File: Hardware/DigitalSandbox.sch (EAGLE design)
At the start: 80 parts, among them J1 AVR_SPI_PRG_6NS, Q1 MOSFET-N, Q2 MOSFET-P, U1 MCP73831, U2 ATMEGA328, U3 C2031N-1A2-B10K-GP, U4 MCP9700, U5 FT232RLSSOP, U6 LIGHTSENSORALS, U7 V_REG_LDOSMD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

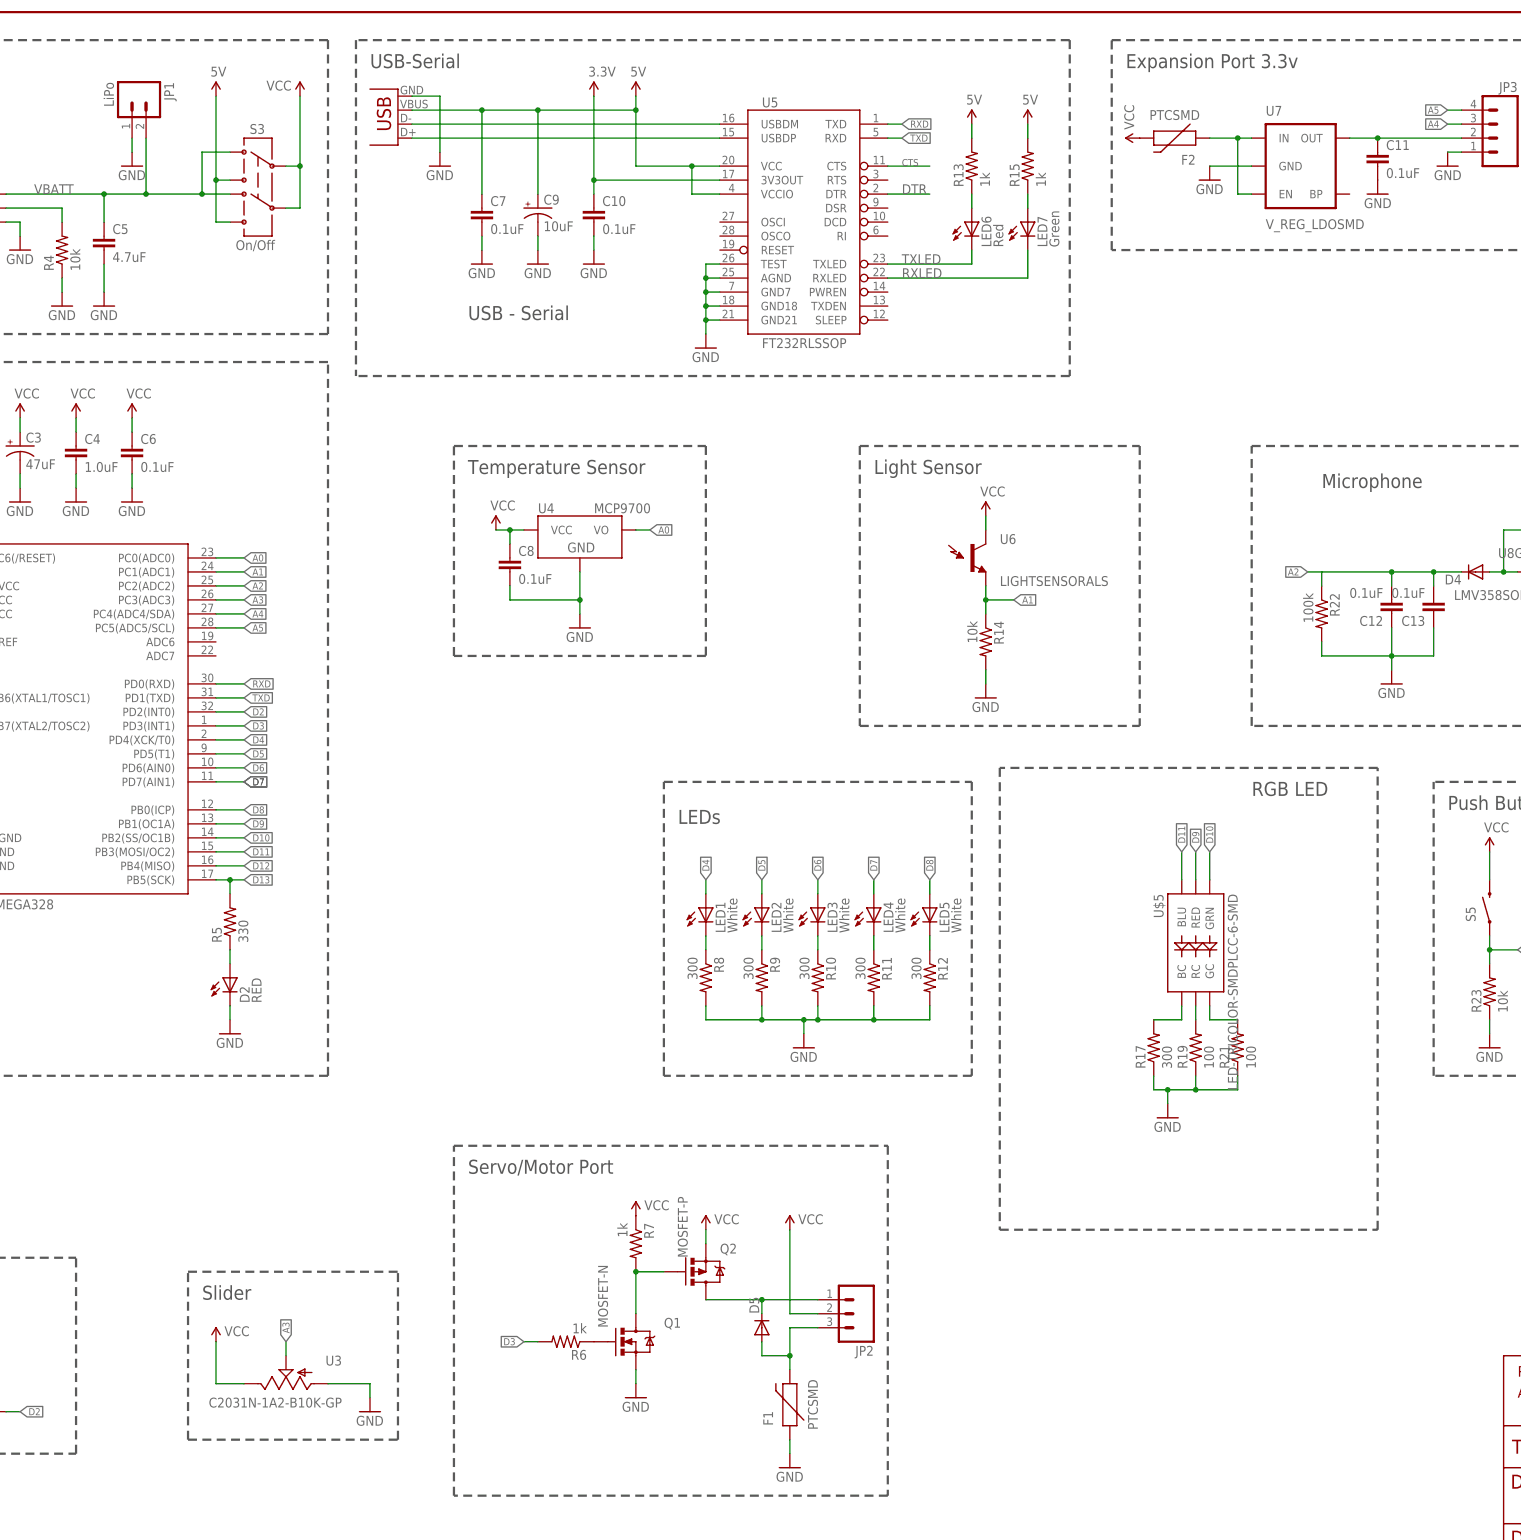
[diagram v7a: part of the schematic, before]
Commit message: updated Sparkle ID's
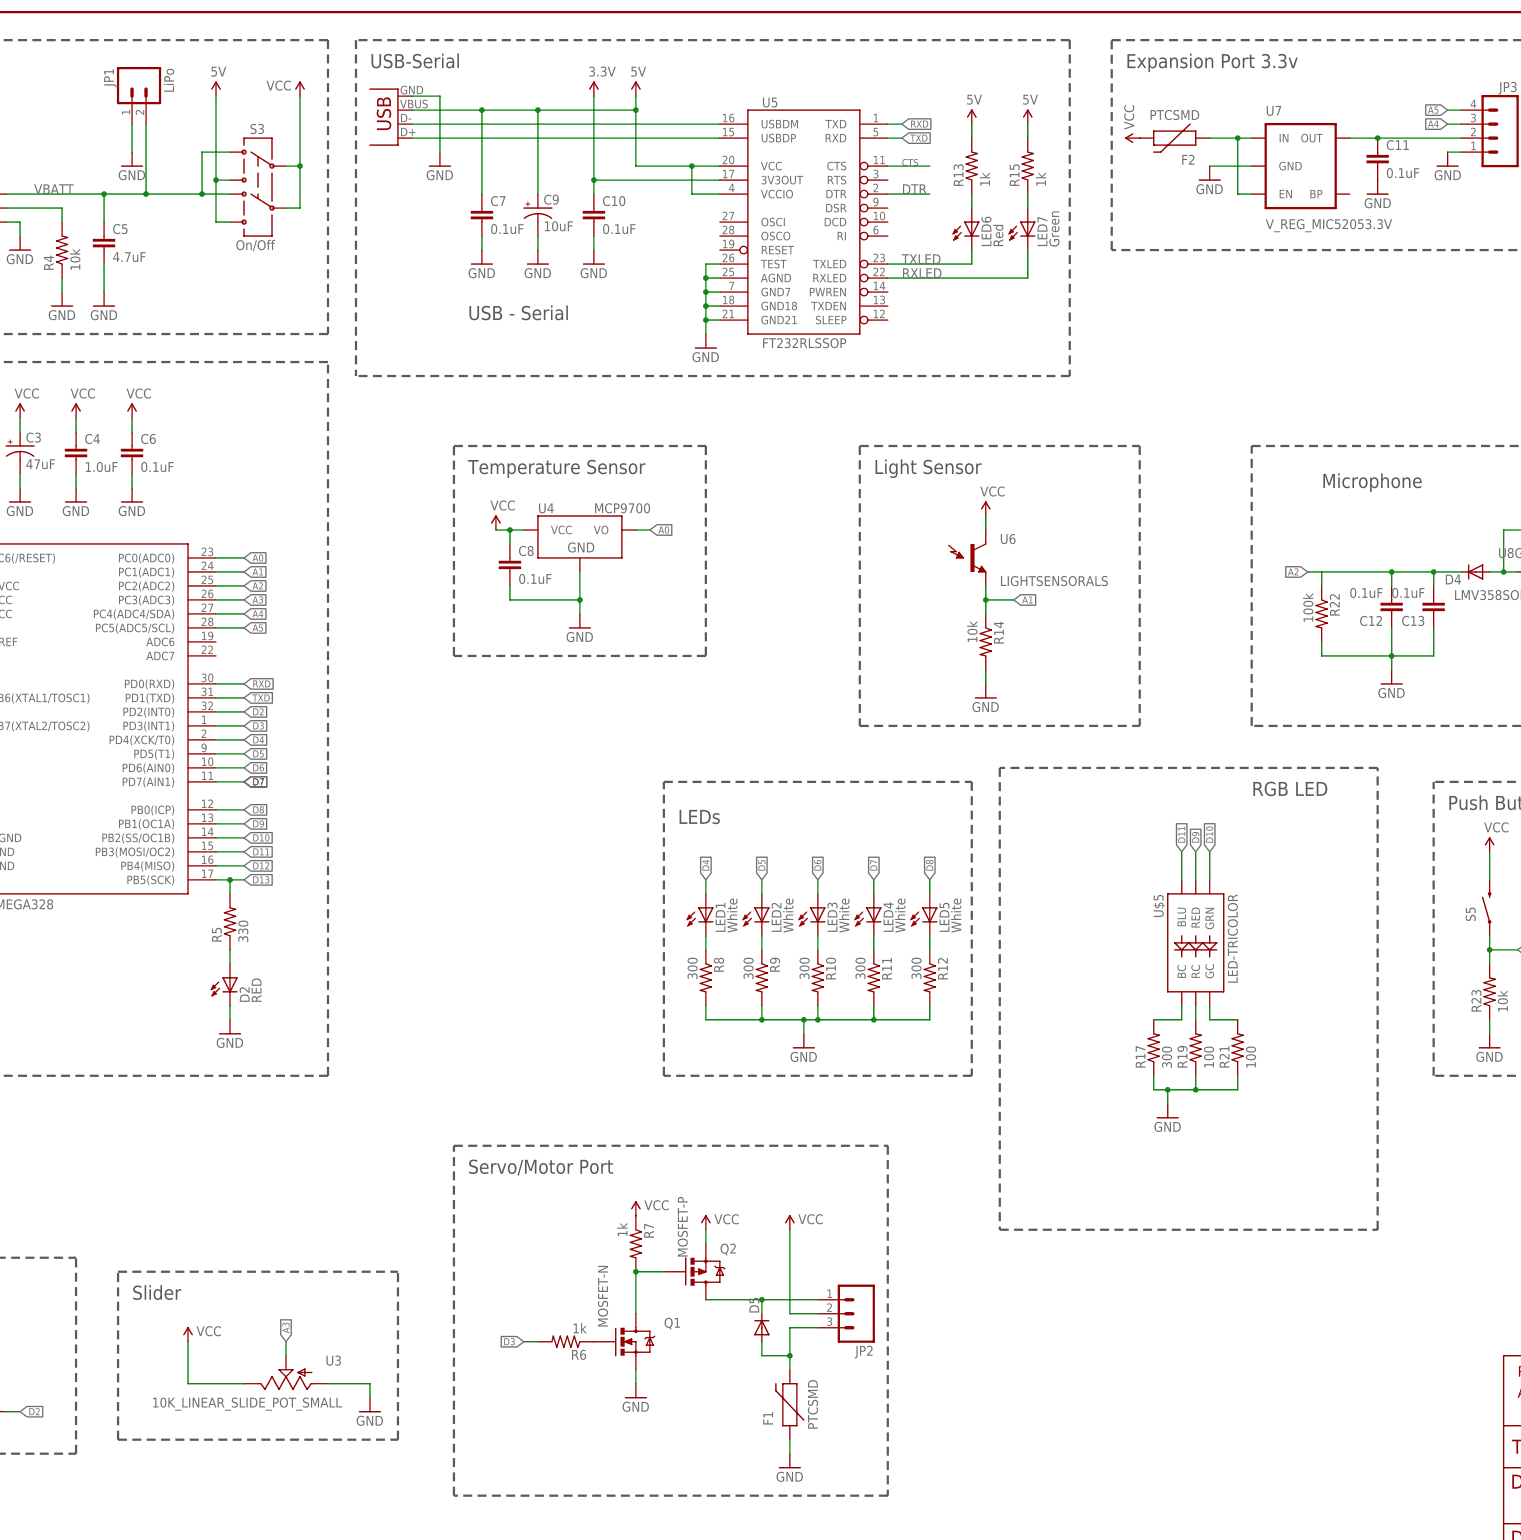
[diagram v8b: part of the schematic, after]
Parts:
- C4: device SparkFun:CAP0603-CAP -> SparkFun-Capacitors:1.0UF-16V-10%(0603)
- JP1: device SparkFun:M02-JST-2MM-SMT -> SparkFun-Connectors:M02-JST-2MM-SMT
- U$5: value LED-TRICOLOR-SMDPLCC-6-SMD -> LED-TRICOLOR; device Testing:LED-TRICOLOR-SMDPLCC-6-SMD -> SparkFun-LED:LED-TRICOLOR-NO-COMPLCC-6-SMD
- U3: value C2031N-1A2-B10K-GP -> 10K_LINEAR_SLIDE_POT_SMALL; device C2031N-1A2-B10K-GP:C2031N-1A2-B10K-GP -> SparkFun-Resistors:10K_LINEAR_SLIDE_POT_SMALL
- U4: device SparkFun:MCP9700SMD -> SparkFun-Sensors:MCP9700SMD
- U7: value V_REG_LDOSMD -> V_REG_MIC52053.3V; device SparkFun-PowerIC:V_REG_LDOSMD -> SparkFun-PowerIC:V_REG_MIC52053.3V
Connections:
- net GND: now also JP1.2; no longer JP1.1
- net VBATT: now also JP1.1; no longer JP1.2
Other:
- moved on the sheet: JP1
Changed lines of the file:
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@@
 <layer number="54" name="bGND_GNDA" color="1" fill="9" visible="no" active="no"/>
 <layer number="56" name="wert" color="7" fill="1" visible="no" active="no"/>
+<layer number="57" name="tCAD" color="7" fill="1" visible="no" active="no"/>
 <layer number="91" name="Nets" color="2" fill="1" visible="yes" active="yes"/>
 <layer number="92" name="Busses" color="1" fill="1" visible="yes" active="yes"/>
@@
 <layer number="97" name="Info" color="7" fill="1" visible="yes" active="yes"/>
 <layer number="98" name="Guide" color="6" fill="1" visible="yes" active="yes"/>
+<layer number="99" name="SpiceOrder" color="7" fill="1" visible="yes" active="yes"/>
 <layer number="100" name="Muster" color="7" fill="1" visible="no" active="no"/>
 <layer number="101" name="Patch_Top" color="12" fill="4" visible="yes" active="yes"/>
@@
 <layer number="132" name="bAdjust" color="7" fill="1" visible="yes" active="yes"/>
 <layer number="144" name="Drill_legend" color="7" fill="1" visible="yes" active="yes"/>
+<layer number="150" name="Notes" color="7" fill="1" visible="yes" active="yes"/>
 <layer number="151" name="HeatSink" color="7" fill="1" visible="yes" active="yes"/>
 <layer number="152" name="_bDocu" color="7" fill="1" visible="yes" active="yes"/>
+<layer number="153" name="FabDoc1" color="7" fill="1" visible="yes" active="yes"/>
+<layer number="154" name="FabDoc2" color="7" fill="1" visible="yes" active="yes"/>
+<layer number="155" name="FabDoc3" color="7" fill="1" visible="yes" active="yes"/>
 <layer number="199" name="Contour" color="7" fill="1" visible="yes" active="yes"/>
 <layer number="200" name="200bmp" color="1" fill="10" visible="no" active="no"/>
@@
 <part name="Y1" library="SparkFun-FreqCtrl" deviceset="RESONATOR" device="8MHZ" value="8MHz"/>
 <part name="GND9" library="SparkFun" deviceset="GND" device=""/>
-<part name="JP1" library="SparkFun" deviceset="M02" device="-JST-2MM-SMT" value="LiPo"/>
+<part name="JP1" library="SparkFun-Connectors" deviceset="M02" device="-JST-2MM-SMT" value="LiPo"/>
 <part name="S3" library="SparkFun-Electromechanical" deviceset="SWITCH-DPDT" device="AYZ0202" value="On/Off"/>
 <part name="GND18" library="supply1" deviceset="GND" device=""/>
@@
 <part name="S1" library="SparkFun-Electromechanical" deviceset="TAC_SWITCH" device="SMD" value="Reset"/>
 <part name="GND13" library="supply1" deviceset="GND" device=""/>
-<part name="U4" library="SparkFun" deviceset="MCP9700" device="SMD" value="MCP9700"/>
+<part name="U4" library="SparkFun-Sensors" deviceset="MCP9700" device="SMD" value="MCP9700"/>
 <part name="C8" library="SparkFun-Capacitors" deviceset="0.1UF-25V(+80/-20%)(0603)" device="" value="0.1uF"/>
 <part name="S2" library="SparkFun-Electromechanical" deviceset="SWITCH-DPDT" device="AYZ0202"/>
@@
 <part name="R11" library="SparkFun-Resistors" deviceset="300OHM-1/10W-1%(0603)" device="" value="300"/>
 <part name="R12" library="SparkFun-Resistors" deviceset="300OHM-1/10W-1%(0603)" device="" value="300"/>
-<part name="U3" library="C2031N-1A2-B10K-GP" deviceset="C2031N-1A2-B10K-GP" device=""/>
+<part name="U3" library="SparkFun-Resistors" deviceset="10K_LINEAR_SLIDE_POT_SMALL" device=""/>
 <part name="R17" library="SparkFun-Resistors" deviceset="300OHM-1/10W-1%(0603)" device="" value="300"/>
 <part name="R19" library="SparkFun-Resistors" deviceset="100OHM1/10W1%(0603)" device="" value="100"/>
@@
 <part name="C6" library="SparkFun-Capacitors" deviceset="0.1UF-25V(+80/-20%)(0603)" device="" value="0.1uF"/>
 <part name="C1" library="SparkFun-Capacitors" deviceset="0.1UF-25V(+80/-20%)(0603)" device="" value="0.1uF"/>
-<part name="C4" library="SparkFun" deviceset="CAP" device="0603-CAP" value="1.0uF"/>
+<part name="C4" library="SparkFun-Capacitors" deviceset="1.0UF-16V-10%(0603)" device="" value="1.0uF"/>
 <part name="GND8" library="SparkFun" deviceset="GND" device=""/>
 <part name="R3" library="SparkFun-Resistors" deviceset="10KOHM1/10W1%(0603)" device="0603" value="10k"/>
@@
 <part name="JP3" library="SparkFun-Connectors" deviceset="M04" device="SMD_STRAIGHT_COMBO"/>
 <part name="GND31" library="SparkFun" deviceset="GND" device=""/>
-<part name="U7" library="SparkFun-PowerIC" deviceset="V_REG_LDO" device="SMD"/>
+<part name="U7" library="SparkFun-PowerIC" deviceset="V_REG_MIC5205" device="3.3V"/>
 <part name="GND32" library="SparkFun" deviceset="GND" device=""/>
 <part name="P+19" library="SparkFun" deviceset="VCC" device=""/>
@@
 <part name="D5" library="SparkFun-DiscreteSemi" deviceset="DIODE" device="SOD"/>
 <part name="D2" library="SparkFun-LED" deviceset="LED-RED" device="1206" value="RED"/>
-<part name="U$5" library="Testing" deviceset="LED-TRICOLOR-SMD" device="PLCC-6-SMD"/>
+<part name="U$5" library="SparkFun-LED" deviceset="LED-TRICOLOR-NO-COM" device="PLCC-6-SMD" value="LED-TRICOLOR"/>
 <part name="S5" library="SparkFun-Electromechanical" deviceset="SWITCH-MOMENTARY-2" device="SMD-4"/>
 <part name="GND34" library="SparkFun" deviceset="GND" device=""/>
@@
 <text x="124.46" y="269.24" size="2.54" layer="97">USB-Serial</text>
 <text x="142.24" y="68.58" size="2.54" layer="97">Servo/Motor Port</text>
-<text x="93.98" y="48.26" size="2.54" layer="97" rot="MR180">Slider</text>
+<text x="81.28" y="48.26" size="2.54" layer="97" rot="MR180">Slider</text>
 <text x="320.04" y="134.62" size="2.54" layer="97">Push Button</text>
 <text x="22.86" y="48.26" size="2.54" layer="97" rot="MR180">Slide Switch</text>
@@
 <wire x1="71.12" y1="17.78" x2="71.12" y2="53.34" width="0.4064" layer="97" style="shortdash"/>
 <wire x1="20.32" y1="53.34" x2="71.12" y2="53.34" width="0.4064" layer="97" style="shortdash"/>
-<wire x1="91.44" y1="50.8" x2="129.54" y2="50.8" width="0.4064" layer="97" style="shortdash"/>
-<wire x1="91.44" y1="20.32" x2="91.44" y2="50.8" width="0.4064" layer="97" style="shortdash"/>
+<wire x1="78.74" y1="50.8" x2="129.54" y2="50.8" width="0.4064" layer="97" style="shortdash"/>
+<wire x1="78.74" y1="20.32" x2="78.74" y2="50.8" width="0.4064" layer="97" style="shortdash"/>
 <wire x1="129.54" y1="20.32" x2="129.54" y2="50.8" width="0.4064" layer="97" style="shortdash"/>
-<wire x1="91.44" y1="20.32" x2="129.54" y2="20.32" width="0.4064" layer="97" style="shortdash"/>
+<wire x1="78.74" y1="20.32" x2="129.54" y2="20.32" width="0.4064" layer="97" style="shortdash"/>
 <wire x1="213.36" y1="200.66" x2="213.36" y2="149.86" width="0.4064" layer="97" style="shortdash"/>
 <wire x1="213.36" y1="149.86" x2="264.16" y2="149.86" width="0.4064" layer="97" style="shortdash"/>
@@
 </instance>
 <instance part="GND9" gate="1" x="33.02" y="147.32"/>
-<instance part="JP1" gate="G$1" x="81.28" y="264.16" rot="R270"/>
+<instance part="JP1" gate="G$1" x="83.82" y="266.7" rot="MR270"/>
 <instance part="S3" gate="G$1" x="104.14" y="248.92" smashed="yes" rot="MR0">
 <attribute name="NAME" x="102.616" y="257.302" size="1.778" layer="95"/>
@@
 <attribute name="VALUE" x="46.736" y="49.276" size="1.778" layer="96" rot="MR0"/>
 </instance>
-<instance part="P+5" gate="1" x="96.52" y="38.1" smashed="yes">
-<attribute name="VALUE" x="98.044" y="39.116" size="1.778" layer="96"/>
+<instance part="P+5" gate="1" x="91.44" y="38.1" smashed="yes">
+<attribute name="VALUE" x="92.964" y="39.116" size="1.778" layer="96"/>
 </instance>
 <instance part="GND14" gate="1" x="124.46" y="25.4"/>
@@
 <instance part="D5" gate="G$1" x="195.58" y="40.64" rot="R90"/>
 <instance part="D2" gate="G$1" x="99.06" y="104.14"/>
-<instance part="U$5" gate="G$1" x="274.32" y="109.22" rot="MR270"/>
+<instance part="U$5" gate="G$1" x="274.32" y="109.22" smashed="yes" rot="MR270">
+<attribute name="NAME" x="268.478" y="119.38" size="1.778" layer="95" rot="MR270"/>
+<attribute name="VALUE" x="281.94" y="119.38" size="1.778" layer="95" rot="MR270"/>
+</instance>
 <instance part="S5" gate="G$1" x="327.66" y="116.84" smashed="yes" rot="R90">
 <attribute name="NAME" x="325.12" y="114.3" size="1.778" layer="95" rot="R90"/>
@@
 <pinref part="GND20" gate="1" pin="GND"/>
 <pinref part="C5" gate="G$1" pin="2"/>
-</segment>
-<segment>
-<wire x1="81.28" y1="256.54" x2="81.28" y2="254" width="0.1524" layer="91"/>
-<pinref part="JP1" gate="G$1" pin="1"/>
-<pinref part="GND12" gate="1" pin="GND"/>
 </segment>
 <segment>
@@
 <junction x="274.32" y="83.82"/>
 </segment>
+<segment>
+<pinref part="GND12" gate="1" pin="GND"/>
+<pinref part="JP1" gate="G$1" pin="2"/>
+<wire x1="81.28" y1="254" x2="81.28" y2="259.08" width="0.1524" layer="91"/>
+</segment>
 </net>
 <net name="VCC" class="1">
@@
 </segment>
 <segment>
-<wire x1="96.52" y1="38.1" x2="96.52" y2="30.48" width="0.1524" layer="91"/>
-<wire x1="96.52" y1="30.48" x2="101.6" y2="30.48" width="0.1524" layer="91"/>
+<wire x1="91.44" y1="38.1" x2="91.44" y2="30.48" width="0.1524" layer="91"/>
+<wire x1="91.44" y1="30.48" x2="101.6" y2="30.48" width="0.1524" layer="91"/>
 <pinref part="U3" gate="G$1" pin="E"/>
 <pinref part="P+5" gate="1" pin="VCC"/>
@@
 <pinref part="C5" gate="G$1" pin="1"/>
 <label x="63.5" y="246.38" size="1.778" layer="95"/>
-<pinref part="JP1" gate="G$1" pin="2"/>
-<wire x1="76.2" y1="246.38" x2="83.82" y2="246.38" width="0.1524" layer="91"/>
-<wire x1="83.82" y1="246.38" x2="83.82" y2="256.54" width="0.1524" layer="91"/>
 <wire x1="93.98" y1="246.38" x2="83.82" y2="246.38" width="0.1524" layer="91"/>
-<junction x="83.82" y="246.38"/>
+<wire x1="83.82" y1="246.38" x2="76.2" y2="246.38" width="0.1524" layer="91"/>
 <wire x1="93.98" y1="246.38" x2="93.98" y2="254" width="0.1524" layer="91"/>
 <pinref part="S3" gate="G$1" pin="1"/>
@@
 <wire x1="93.98" y1="246.38" x2="99.06" y2="246.38" width="0.1524" layer="91"/>
 <junction x="93.98" y="246.38"/>
-</segment>
-</net>
+<pinref part="JP1" gate="G$1" pin="1"/>
+<wire x1="83.82" y1="259.08" x2="83.82" y2="246.38" width="0.1524" layer="91"/>
+<junction x="83.82" y="246.38"/>
+</segment>
+</net>
